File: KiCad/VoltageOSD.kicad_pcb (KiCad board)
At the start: 2 copper layers, 8.6 x 6.2 mm, 18 parts, among them J1 Camera, J2 VTX, J3 RST, J4 SCK, J5 MOSI, U1 LMH1980, U2 ATTINY13A-MMF

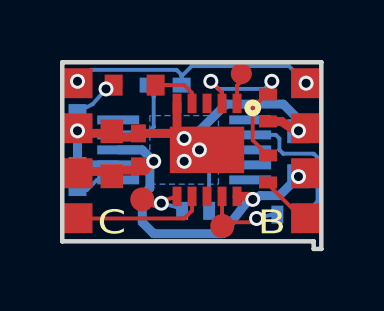
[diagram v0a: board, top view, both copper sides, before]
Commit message: change schematic for INT0. Add ASM project.
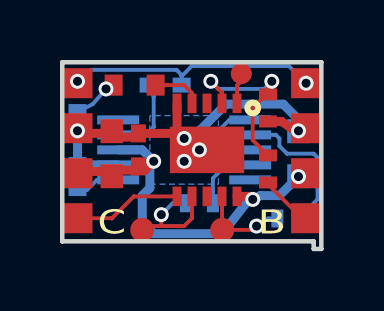
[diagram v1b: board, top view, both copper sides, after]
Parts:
- J4: value SCK -> MISO
- J5: value MOSI -> SCK
- moved R6 3.19 mm to (150.9, 115.7)
- moved R5 3.07 mm to (147.8, 115.2)
- moved J5 2.85 mm to (148.6, 116.1)
- moved J4 2.67 mm to (145.9, 116.1)
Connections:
- U1 pad 6: Net-(U1-Pad6) -> Net-(R5-Pad1)
- U1 pad 7: Net-(R5-Pad1) -> Net-(R6-Pad1)
- U1 pad 8: Net-(R6-Pad1) -> Net-(U1-Pad8)
- U2 pad 11: GND -> (no net)
- U2 pad 6: Net-(J5-Pad1) -> CONFIGURE
- U2 pad 7: CONFIGURE -> Net-(J4-Pad1)
- U2 pad 9: Net-(J4-Pad1) -> Net-(J5-Pad1)
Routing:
- net GND: track 16.8 -> 19.6 mm
- net Net-(R6-Pad1): track 2.94 -> 4.93 mm
- net Net-(J4-Pad1): track 2.62 -> 3.98 mm
- net Net-(J5-Pad1): track 1.87 -> 3.09 mm
- net Net-(R5-Pad1): track 4.87 -> 3.70 mm

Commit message: Final Schematic and PCB (sent to OshPark)
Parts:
- added R7: 100, Resistors_SMD:R_0402_NoSilk, F.Cu at (145.4, 115.1)
- R3: value 150K -> 15K
- R4: value 10K -> 1K
- moved C3 0.25 mm to (144.9, 113.3)
- moved J4 0.25 mm to (146.2, 116.1)
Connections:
- U2 pad 6: CONFIGURE -> Net-(R7-Pad2)
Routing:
- net CONFIGURE: track 4.12 -> 2.01 mm
- net Net-(R7-Pad2): track 0.00 -> 1.26 mm
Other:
- rule pad_to_mask_clearance: 0.1 -> 0.08
- board text added: "B-uOSD"
- board text removed: "B-OSD"

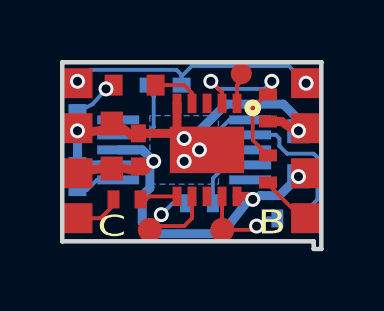
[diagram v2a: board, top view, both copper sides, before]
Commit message: Adjusted schematic and PCB (not critical values)
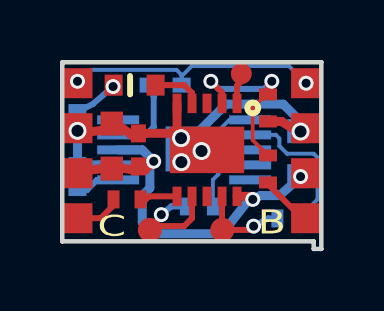
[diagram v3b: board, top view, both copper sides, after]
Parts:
- added REF**: Measurement_Point_Square-SMD-Pad_Small, Measurement_Points:Measurement_Point_Square-SMD-Pad_Small, B.Cu at (147.4, 113.4)
- R2: value 120 -> 220
- R5, R6, R7: value 100 -> 120
- moved R5 0.11 mm to (147.8, 115.3)
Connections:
- U2 pad 11: (no net) -> GND
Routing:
- net GND: track 19.8 -> 23.1 mm
- removed copper zone on B.Cu, net GND
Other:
- net class Default: trace_width 0.13 -> 0.2
- net class GND: via_dia 0.5 -> 0.6; via_drill 0.3 -> 0.4
- net class ProgLine added: clearance 0.13, trace_width 0.2, via_dia 0.5, via_drill 0.3
- net class Thin added: clearance 0.13, trace_width 0.13, via_dia 0.5, via_drill 0.3
